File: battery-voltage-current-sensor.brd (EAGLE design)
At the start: 100 x 100 mm, 66 parts, among them IC1 ACS758LCB-050B-PFF-T, IC3 ADS1115IDGST, T1 C8545, T2 C8545, T3 C8545, X1 MKDSN1,5/2-5,08

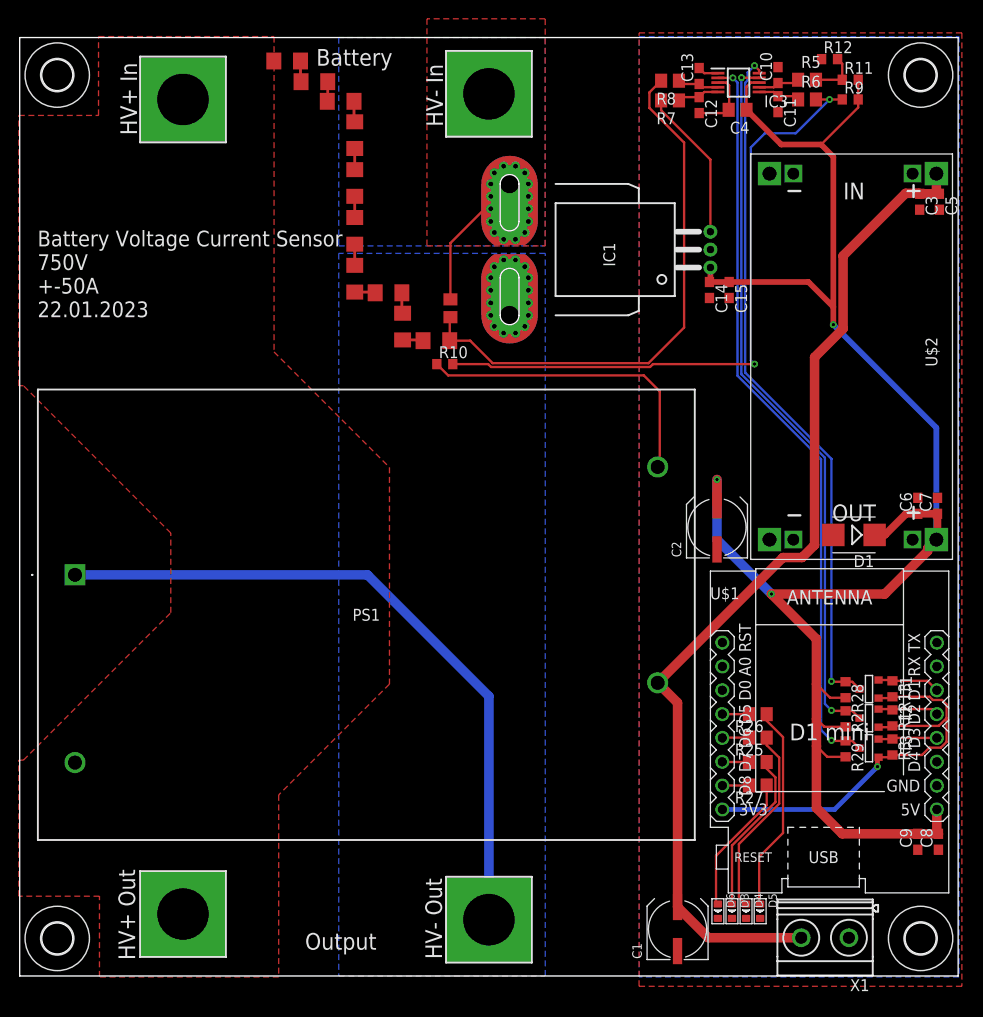
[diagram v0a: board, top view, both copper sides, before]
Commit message: capacitors moved
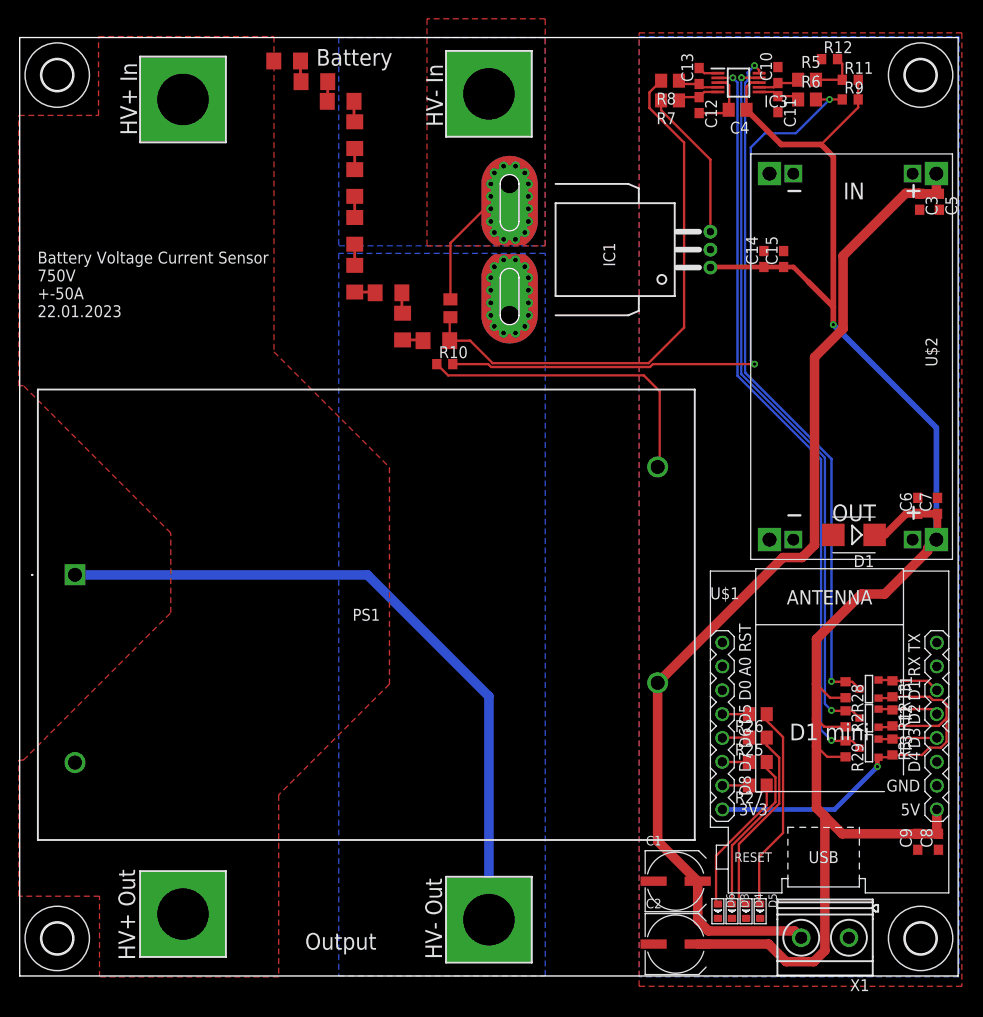
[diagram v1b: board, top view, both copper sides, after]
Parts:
- moved C2 44.6 mm to (69.9, 3.40), turned to 0 degrees
- moved C15 6.67 mm to (81.4, 76.4), turned to 90 degrees
- moved C14 6.67 mm to (79.3, 76.4), turned to 90 degrees
- moved C1 5.10 mm to (69.9, 10.1), turned to 0 degrees
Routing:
- net +5V/1: track 185.3 -> 186.5 mm, vias 3 -> 1
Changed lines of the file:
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@@
 <rectangle x1="24" y1="43.3" x2="34" y2="163.3" layer="42"/>
 <circle x="5.8" y="43" radius="10" width="0" layer="41"/>
-<text x="1.9" y="70.2" size="1.6764" layer="25">Battery Voltage Current Sensor
+<text x="1.9" y="70.2" size="1.27" layer="25">Battery Voltage Current Sensor
 750V
 +-50A
@@
 <attribute name="VALUE" x="82.55" y="66.5" size="1.27" layer="27" rot="R270" align="top-center"/>
 </element>
-<element name="C1" library="rcl" library_urn="urn:adsk.eagle:library:334" package="UD-6,3X7,7_NICHICON" package3d_urn="urn:adsk.eagle:package:23472/1" value="C473426" x="70.1" y="5" smashed="yes" rot="R90">
-<attribute name="NAME" x="66.29" y="1.825" size="1.016" layer="25" rot="R90"/>
-<attribute name="VALUE" x="74.545" y="1.825" size="1.016" layer="27" rot="R90"/>
-</element>
-<element name="C2" library="rcl" library_urn="urn:adsk.eagle:library:334" package="UD-6,3X7,7_NICHICON" package3d_urn="urn:adsk.eagle:package:23472/1" value="C473426" x="74.3" y="47.8" smashed="yes" rot="R90">
-<attribute name="NAME" x="70.49" y="44.625" size="1.016" layer="25" rot="R90"/>
-<attribute name="VALUE" x="78.745" y="44.625" size="1.016" layer="27" rot="R90"/>
+<element name="C1" library="rcl" library_urn="urn:adsk.eagle:library:334" package="UD-6,3X7,7_NICHICON" package3d_urn="urn:adsk.eagle:package:23472/1" value="C473426" x="69.9" y="10.1" smashed="yes">
+<attribute name="NAME" x="66.725" y="13.91" size="1.016" layer="25"/>
+<attribute name="VALUE" x="66.725" y="5.655" size="1.016" layer="27"/>
+</element>
+<element name="C2" library="rcl" library_urn="urn:adsk.eagle:library:334" package="UD-6,3X7,7_NICHICON" package3d_urn="urn:adsk.eagle:package:23472/1" value="C473426" x="69.9" y="3.4" smashed="yes">
+<attribute name="NAME" x="66.725" y="7.21" size="1.016" layer="25"/>
+<attribute name="VALUE" x="66.725" y="-1.045" size="1.016" layer="27"/>
 </element>
 <element name="C3" library="rcl" library_urn="urn:adsk.eagle:library:334" package="C0603" package3d_urn="urn:adsk.eagle:package:23616/2" value="100nF" x="95.9" y="82.5" smashed="yes" rot="R270">
@@
 <attribute name="VALUE" x="69.935" y="97.94" size="1.27" layer="27" rot="R180"/>
 </element>
-<element name="C14" library="rcl" library_urn="urn:adsk.eagle:library:334" package="C0603" package3d_urn="urn:adsk.eagle:package:23616/2" value="100nF" x="73.5" y="73.1" smashed="yes" rot="R270">
-<attribute name="NAME" x="74.135" y="73.735" size="1.27" layer="25" rot="R270"/>
-<attribute name="VALUE" x="71.595" y="73.735" size="1.27" layer="27" rot="R270"/>
-</element>
-<element name="C15" library="rcl" library_urn="urn:adsk.eagle:library:334" package="C0603" package3d_urn="urn:adsk.eagle:package:23616/2" value="100nF" x="75.6" y="73.1" smashed="yes" rot="R270">
-<attribute name="NAME" x="76.235" y="73.735" size="1.27" layer="25" rot="R270"/>
-<attribute name="VALUE" x="73.695" y="73.735" size="1.27" layer="27" rot="R270"/>
+<element name="C14" library="rcl" library_urn="urn:adsk.eagle:library:334" package="C0603" package3d_urn="urn:adsk.eagle:package:23616/2" value="100nF" x="79.3" y="76.4" smashed="yes" rot="R90">
+<attribute name="NAME" x="78.665" y="75.765" size="1.27" layer="25" rot="R90"/>
+<attribute name="VALUE" x="81.205" y="75.765" size="1.27" layer="27" rot="R90"/>
+</element>
+<element name="C15" library="rcl" library_urn="urn:adsk.eagle:library:334" package="C0603" package3d_urn="urn:adsk.eagle:package:23616/2" value="100nF" x="81.4" y="76.4" smashed="yes" rot="R90">
+<attribute name="NAME" x="80.765" y="75.765" size="1.27" layer="25" rot="R90"/>
+<attribute name="VALUE" x="83.305" y="75.765" size="1.27" layer="27" rot="R90"/>
 </element>
 <element name="R9" library="rcl" library_urn="urn:adsk.eagle:library:334" package="R0603" package3d_urn="urn:adsk.eagle:package:23555/2" value="10k" x="88.5" y="93.4" smashed="yes">
@@
 <wire x1="81.15" y1="88.6" x2="85.4" y2="88.6" width="0.6096" layer="1"/>
 <wire x1="86.7" y1="87.3" x2="85.4" y2="88.6" width="0.6096" layer="1"/>
-<wire x1="73.6" y1="75.49" x2="73.6" y2="74.05" width="0.6096" layer="1"/>
-<wire x1="73.6" y1="74.05" x2="73.5" y2="73.95" width="0.6096" layer="1"/>
-<wire x1="73.5" y1="73.95" x2="75.6" y2="73.95" width="0.6096" layer="1"/>
-<wire x1="75.6" y1="73.95" x2="84.05" y2="73.95" width="0.6096" layer="1"/>
-<wire x1="84.05" y1="73.95" x2="86.7" y2="71.3" width="0.6096" layer="1"/>
+<wire x1="86.7" y1="71.3" x2="84.05" y2="73.95" width="0.6096" layer="1"/>
 <wire x1="86.7" y1="71.3" x2="86.7" y2="87.3" width="0.6096" layer="1"/>
 <wire x1="86.7" y1="71.3" x2="86.7" y2="69.4" width="0.6096" layer="1"/>
@@
 <contactref element="R2" pad="2"/>
 <contactref element="R29" pad="2"/>
-<via x="80.1" y="40.7" extent="1-16" drill="0.35"/>
 <wire x1="97.68" y1="46.5" x2="96.7529" y2="45.5729" width="1.016" layer="1"/>
 <wire x1="96.7529" y1="45.5729" x2="96.7529" y2="45.27395625" width="1.016" layer="1"/>
-<wire x1="96.7529" y1="45.27395625" x2="92.17894375" y2="40.7" width="1.016" layer="1"/>
-<wire x1="92.17894375" y1="40.7" x2="80.1" y2="40.7" width="1.016" layer="1"/>
-<wire x1="80.1" y1="40.7" x2="74.3" y2="46.5" width="1.016" layer="16"/>
-<wire x1="74.3" y1="46.5" x2="74.3" y2="52.9" width="1.016" layer="16"/>
-<via x="74.3" y="52.9" extent="1-16" drill="0.35"/>
-<wire x1="74.3" y1="52.9" x2="74.3" y2="50.15" width="1.016" layer="1"/>
-<wire x1="80.1" y1="40.7" x2="84.9" y2="35.9" width="1.016" layer="1"/>
-<wire x1="84.9" y1="35.9" x2="84.9" y2="31.1" width="1.016" layer="1"/>
+<wire x1="92.17894375" y1="40.7" x2="96.7529" y2="45.27395625" width="1.016" layer="1"/>
+<wire x1="84.9" y1="31.1" x2="84.9" y2="35.9" width="1.016" layer="1"/>
 <wire x1="84.9" y1="31.1" x2="84.9" y2="27.4" width="1.016" layer="1"/>
 <wire x1="84.9" y1="27.4" x2="84.9" y2="24.5" width="1.016" layer="1"/>
 <wire x1="84.9" y1="24.5" x2="84.9" y2="17.9" width="1.016" layer="1"/>
-<wire x1="84.9" y1="17.9" x2="87.65" y2="15.15" width="1.016" layer="1"/>
+<wire x1="85.8" y1="17" x2="87.65" y2="15.15" width="1.016" layer="1"/>
 <wire x1="87.65" y1="15.15" x2="95.7" y2="15.15" width="1.016" layer="1"/>
 <wire x1="88" y1="26.55" x2="85.75" y2="26.55" width="0.254" layer="1"/>
@@
 <wire x1="88" y1="29.65" x2="86.35" y2="29.65" width="0.254" layer="1"/>
 <wire x1="86.35" y1="29.65" x2="84.9" y2="31.1" width="0.254" layer="1"/>
+<wire x1="84.05" y1="73.95" x2="82.45" y2="75.55" width="0.508" layer="1"/>
+<wire x1="82.45" y1="75.55" x2="81.4" y2="75.55" width="0.508" layer="1"/>
+<wire x1="81.4" y1="75.55" x2="79.3" y2="75.55" width="0.508" layer="1"/>
+<wire x1="79.3" y1="75.55" x2="73.66" y2="75.55" width="0.508" layer="1"/>
+<wire x1="73.66" y1="75.55" x2="73.6" y2="75.49" width="0.508" layer="1"/>
+<wire x1="72.25" y1="3.4" x2="79.8" y2="3.4" width="1.016" layer="1"/>
+<wire x1="79.8" y1="3.4" x2="81.676" y2="1.524" width="1.016" layer="1"/>
+<wire x1="85.8" y1="17" x2="84.9" y2="17.9" width="1.016" layer="1"/>
+<wire x1="81.676" y1="1.524" x2="84.624" y2="1.524" width="1.016" layer="1"/>
+<wire x1="84.624" y1="1.524" x2="85.8" y2="2.7" width="1.016" layer="1"/>
+<wire x1="85.8" y1="2.7" x2="85.8" y2="17" width="1.016" layer="1"/>
+<wire x1="84.9" y1="35.9" x2="89.7" y2="40.7" width="1.016" layer="1"/>
+<wire x1="89.7" y1="40.7" x2="92.17894375" y2="40.7" width="1.016" layer="1"/>
 </signal>
 <signal name="SCL">
@@
 <wire x1="98" y1="83.35" x2="97.68" y2="83.67" width="1.016" layer="1"/>
 <wire x1="97.68" y1="83.67" x2="97.68" y2="85.5" width="1.016" layer="1"/>
-<wire x1="70.1" y1="7.35" x2="70.1" y2="29.12" width="1.016" layer="1"/>
-<wire x1="70.1" y1="29.12" x2="67.98" y2="31.24" width="1.016" layer="1"/>
 <contactref element="X1" pad="2"/>
-<wire x1="70.1" y1="7.35" x2="73.375" y2="4.075" width="1.016" layer="1"/>
-<wire x1="73.375" y1="4.075" x2="83.2811" y2="4.075" width="1.016" layer="1"/>
 <wire x1="67.98" y1="31.24" x2="81.3296" y2="44.5896" width="1.016" layer="1"/>
 <wire x1="81.3296" y1="44.5896" x2="83.36854375" y2="44.5896" width="1.016" layer="1"/>
@@
 <wire x1="95.85" y1="83.4" x2="95.9" y2="83.35" width="1.016" layer="1"/>
 <wire x1="84.7" y1="45.92105625" x2="84.7" y2="65.93119375" width="1.016" layer="1"/>
+<wire x1="67.98" y1="31.24" x2="67.98" y2="14.37" width="1.016" layer="1"/>
+<wire x1="67.98" y1="14.37" x2="72.25" y2="10.1" width="1.016" layer="1"/>
+<wire x1="72.25" y1="10.1" x2="72.25" y2="5.95" width="1.016" layer="1"/>
+<wire x1="82.5561" y1="4.8" x2="83.2811" y2="4.075" width="1.016" layer="1"/>
+<wire x1="72.25" y1="5.95" x2="73.4" y2="4.8" width="1.016" layer="1"/>
+<wire x1="73.4" y1="4.8" x2="82.5561" y2="4.8" width="1.016" layer="1"/>
 </signal>
 <signal name="AIN3">
@@
 <wire x1="79.6" y1="27.9" x2="79.6" y2="27.19513125" width="0.254" layer="1"/>
 <wire x1="79.6" y1="27.19513125" x2="81.3422" y2="25.45293125" width="0.254" layer="1"/>
-<wire x1="81.3422" y1="25.45293125" x2="81.3422" y2="15.2422" width="0.254" layer="1"/>
+<wire x1="81.3422" y1="25.45293125" x2="81.3422" y2="19.8" width="0.254" layer="1"/>
+<wire x1="81.3422" y1="19.8" x2="81.3422" y2="15.2422" width="0.254" layer="1"/>
 <wire x1="81.3422" y1="15.2422" x2="78.8" y2="12.7" width="0.254" layer="1"/>
 <wire x1="78.8" y1="12.7" x2="78.8" y2="7.762" width="0.254" layer="1"/>
